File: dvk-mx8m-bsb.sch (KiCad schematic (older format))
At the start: 11 parts, among them J101 IMX8M-SOM

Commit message: Have the charge controller IC handle the USB-C DRP PD switch mechanism, notes added on what procedure is required to operate as sink/source and how to swap between these roles
The mainline kernel's TCPM implementation needs to be used in conjunction with the charge controller IC's interface. For example, if the TCPC (PTN5110HQ CC controller) has the USB configured as a sink role then the TCPM (i.MX8M) would read out the CC_STATUS and POWER_STATUS registers of the CC controller IC to know this is the case, and then it (i.MX8M) would configure the charge controller IC accordingly (sink current from VBUS).

Both the CC controller and charge controller's open-drain output interrupt pins are tied together, which means if either of them pull the line low then the i.MX8M needs to check both of their fault registers to determine if a fault has occured on either chip. If the INT pin wasn't pulled low due to a fault then a status update event from either chip may have triggered it, which needs to be determined, as well as the corresponding action taken. These INT pins may need to be separated if the software side is too complex, so long as there's a spare interrupt pins available.

Fast swap is not supported, and is not a requirement.
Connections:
- net labels added: EN_SNK, EN_SRC
- net labels removed: ILIM_5V_VBUS, USB_SNK_SRC, ~CE, ~CHRG_INT
- no-connect marks 22 -> 19

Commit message: Modify the boot config pins such that the eMMC is an 8-bit bus, depressing a momentary push button switch during boot causes SD boot, and relevant options
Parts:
- added J102: TEST_1P, symbol TEST_1P
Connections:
- net labels added: BTN1, BTN2, GPIO1_IO13, NVCC_SD2, PWR_EN, SYS_~RST
- net labels removed: GPIO1_IO13(USB1_OTG_OC), NVCC_SD2_1V8_3V3
- wire segments 330 -> 339
- no-connect marks 19 -> 20
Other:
- note added: "CAPTOUCH_~RST"
- note added: "SAI1_RXD1(GPIO4_IO03)"
- note added: "SAI1_TXD3(GPIO4_IO15)"
- note added: "SAI1_TXD6(GPIO4_IO18)"
- note added: "SAI6_RXD0"
- note added: "SAI6_TXC/RXC"
- note added: "SAI6_TXD0"
- note added: "SAI6_TXFS/RXFS"
- note added: "SW_BACK"
- note added: "SW_HOME"
- note added: "TODO!!!"
- note added: "used to be:"
- note removed: "Comes from POR/Supervisory IC\nbut not the SoC\n(PMIC_STBY_REQ is unavailable)"

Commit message: Begin USB 2.0 hub circuit for M.2 modules, remove supervisory/voltage monitor/watchdog circuit since the EmCraft SoM implements it
USB 2.0 hub circuit still needs to be completed.
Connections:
- net 3V3_P is gone; now on net 3V3_OUT: R101.1, R102.1, R103.1, R104.1
- net GPIO1_IO02(~WDOG~) renamed ~WDG

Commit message: Complete more of the USB hub circuit, connect one of the downstream ports to the WWAN M.2 module, remove the unused VBUS rail, add notes regarding the USB-C port having its corresponding ID pin pulled low
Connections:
- net USB2_DN: now reaches J101.D56 (Pin_56)
- net USB2_DP: now reaches J101.D58 (Pin_58)
- net USB2_VBUS: now reaches J101.D73 (Pin_73)
- net USB2_ID: now reaches J101.D75 (Pin_75)
- no-connect marks 20 -> 19
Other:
- note added: "TODO!!!\nUSB2_VBUS=3.3V???"

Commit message: Begin WiFi+BT M.2 socket circuit, connect the associated USB bus from the hub circuit, determined that the i.MX8M's UART's default POR state is such that CTS is an output and RTS is an input and assigned the signals accordingly
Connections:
- no-connect marks 19 -> 24

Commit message: * added footprints * changes in library to make footprints usable (esp. numbering scheme of SOM9 * assigned footprints to schematic symbols
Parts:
- J101: footprint (none) -> dvk-mx8m-bsb:IMX8M_SOM_EmCr
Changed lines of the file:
@@
 F 0 "J101" H 9050 6300 50  0000 C CNN
 F 1 "IMX8M-SOM" H 9050 2200 50  0000 C CNN
-F 2 "" H 8850 4300 50  0001 C CNN
+F 2 "dvk-mx8m-bsb:IMX8M_SOM_EmCr" H 8850 4300 50  0001 C CNN
 F 3 "" H 8850 4300 50  0001 C CNN
 	1    9050 4300
@@
 F 0 "J101" H 9050 12800 50  0000 C CNN
 F 1 "IMX8M-SOM" H 9050 8700 50  0000 C CNN
-F 2 "" H 8850 10800 50  0001 C CNN
+F 2 "dvk-mx8m-bsb:IMX8M_SOM_EmCr" H 8850 10800 50  0001 C CNN
 F 3 "" H 8850 10800 50  0001 C CNN
 	2    9050 10800
@@
 F 0 "J101" H 15600 6300 50  0000 C CNN
 F 1 "IMX8M-SOM" H 15600 2200 50  0000 C CNN
-F 2 "" H 15400 4300 50  0001 C CNN
+F 2 "dvk-mx8m-bsb:IMX8M_SOM_EmCr" H 15400 4300 50  0001 C CNN
 F 3 "" H 15400 4300 50  0001 C CNN
 	3    15600 4300
@@
 F 0 "J101" H 15600 12800 50  0000 C CNN
 F 1 "IMX8M-SOM" H 15600 8700 50  0000 C CNN
-F 2 "" H 15400 10800 50  0001 C CNN
+F 2 "dvk-mx8m-bsb:IMX8M_SOM_EmCr" H 15400 10800 50  0001 C CNN
 F 3 "" H 15400 10800 50  0001 C CNN
 	4    15600 10800

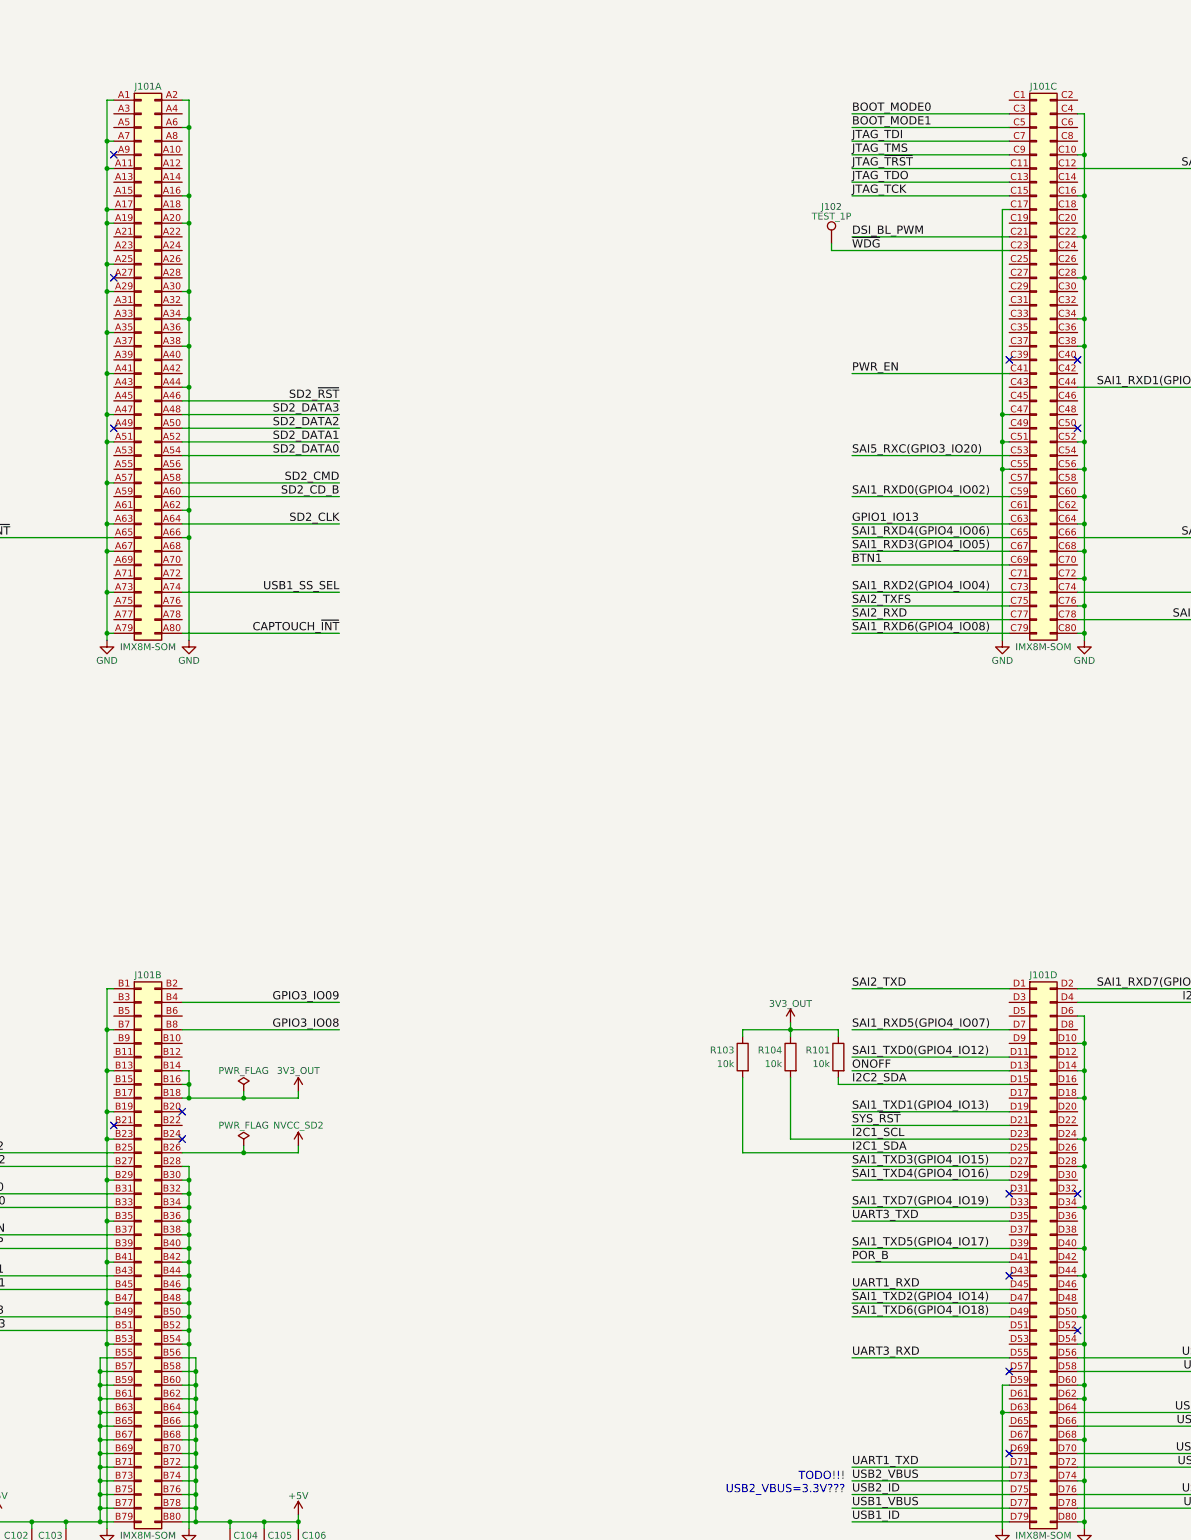
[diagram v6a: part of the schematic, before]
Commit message: Add MicroSD footprint from selection, add PDF file with searchable/highlightable text
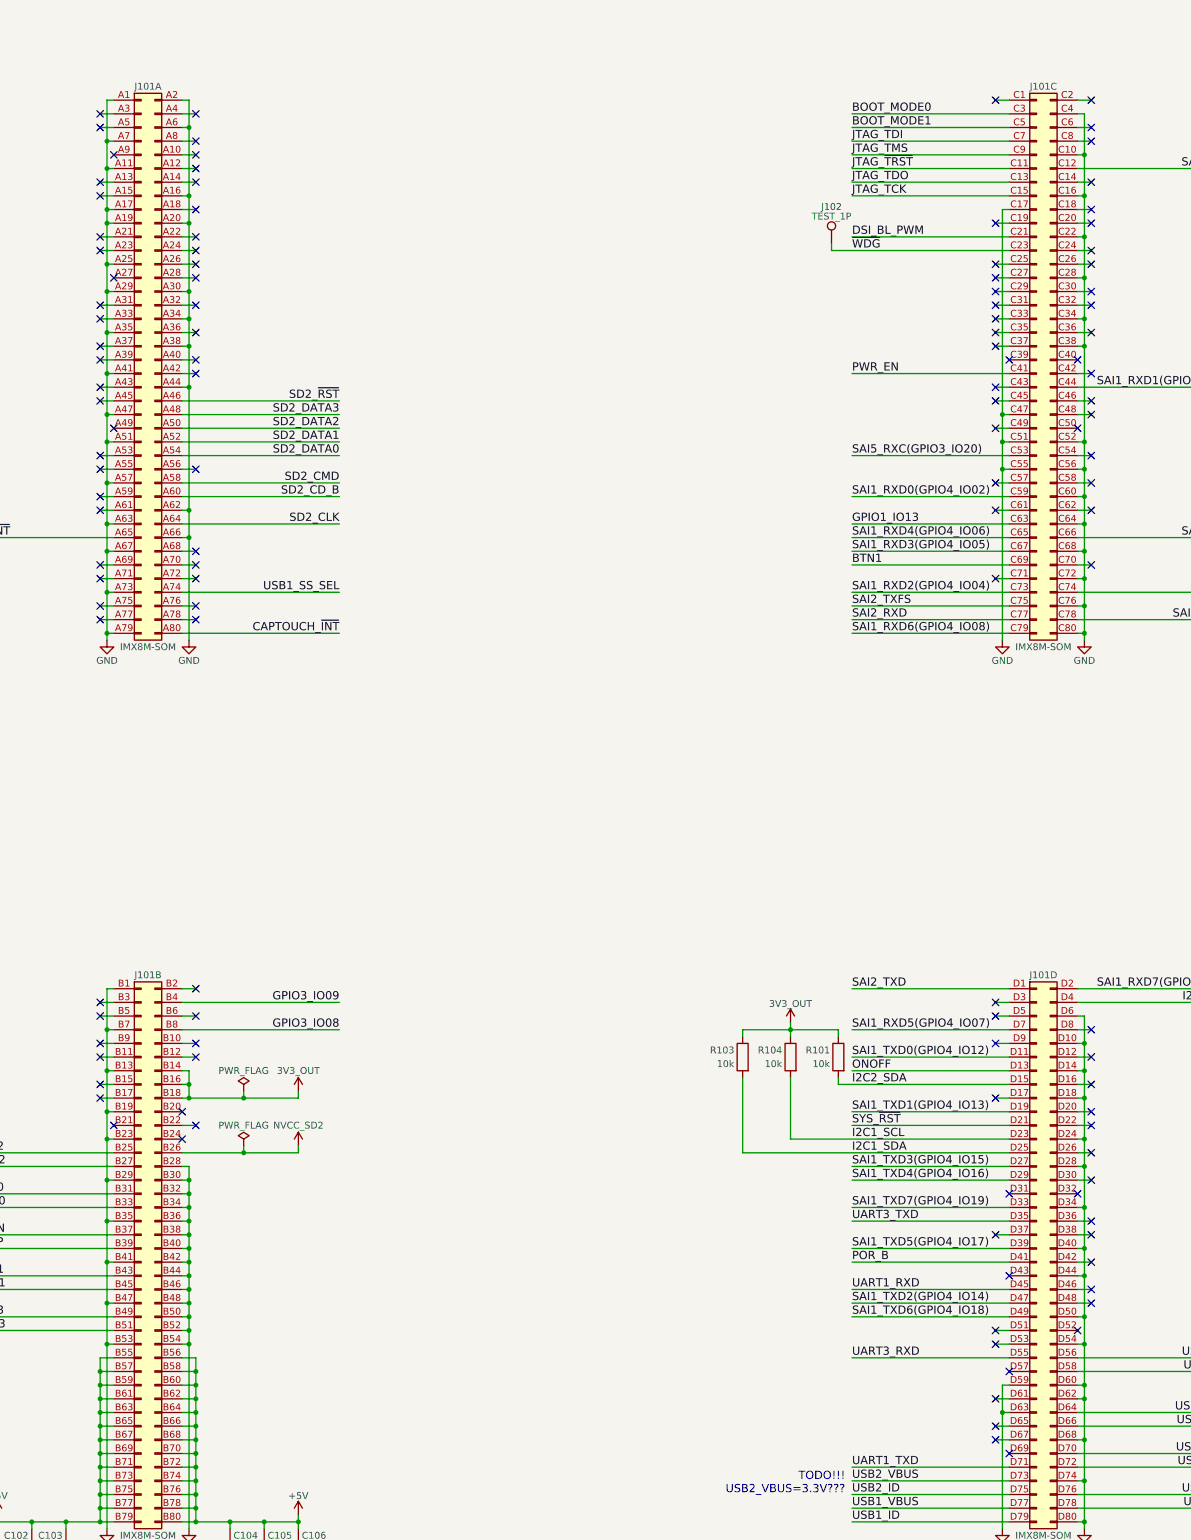
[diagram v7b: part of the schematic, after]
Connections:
- no-connect marks 24 -> 130
